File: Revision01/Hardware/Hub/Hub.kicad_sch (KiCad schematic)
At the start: 26 parts, among them J20 Conn_01x04, J3 Conn_01x04, J4 Conn_01x05, J5 Conn_01x05, SW1 ON/OFF_SW_SPST_LED, U1 NUCLEO-L476RG, U2 LMR51603XFDBVR

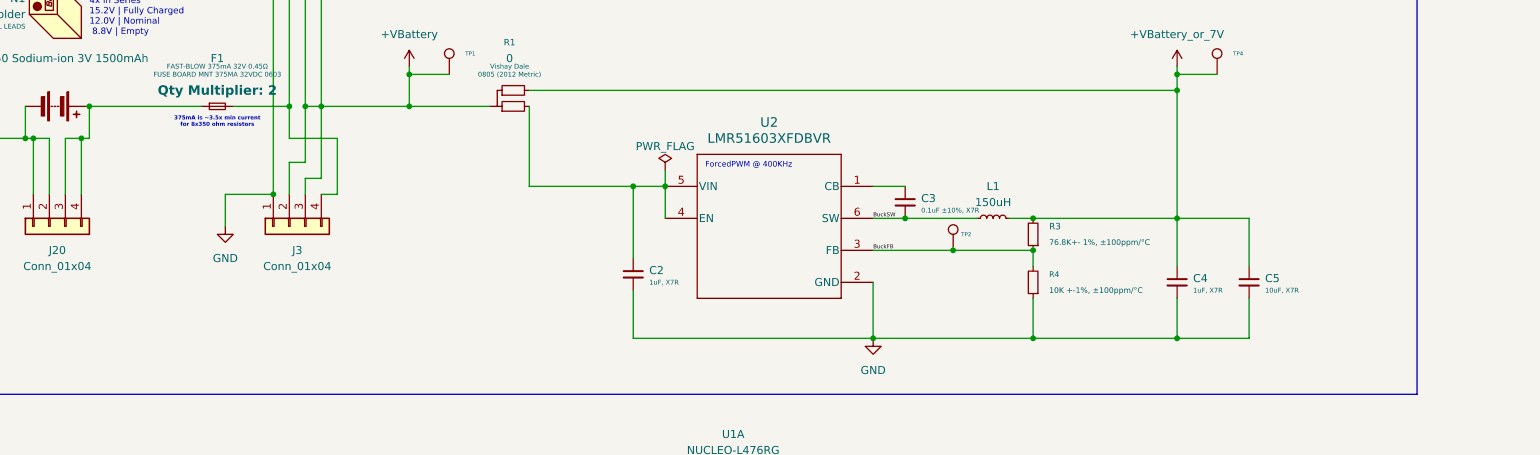
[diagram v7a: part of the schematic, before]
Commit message: . Hub & Amp: Changed wiring standard to GND SIG GND GND PWR GND . Hub: Added GND plane to 3.3V . Hub: Moved 1M pulldown resistor . Hub & Amp: Adjusted thermal relief tolerances . Hub: Changed buck convertor layout so capacitors are inline with feedback pin . Hub: Added stitching vias . Hub & Amp: Changed font sizes, changed silkscreen to be oriented one way
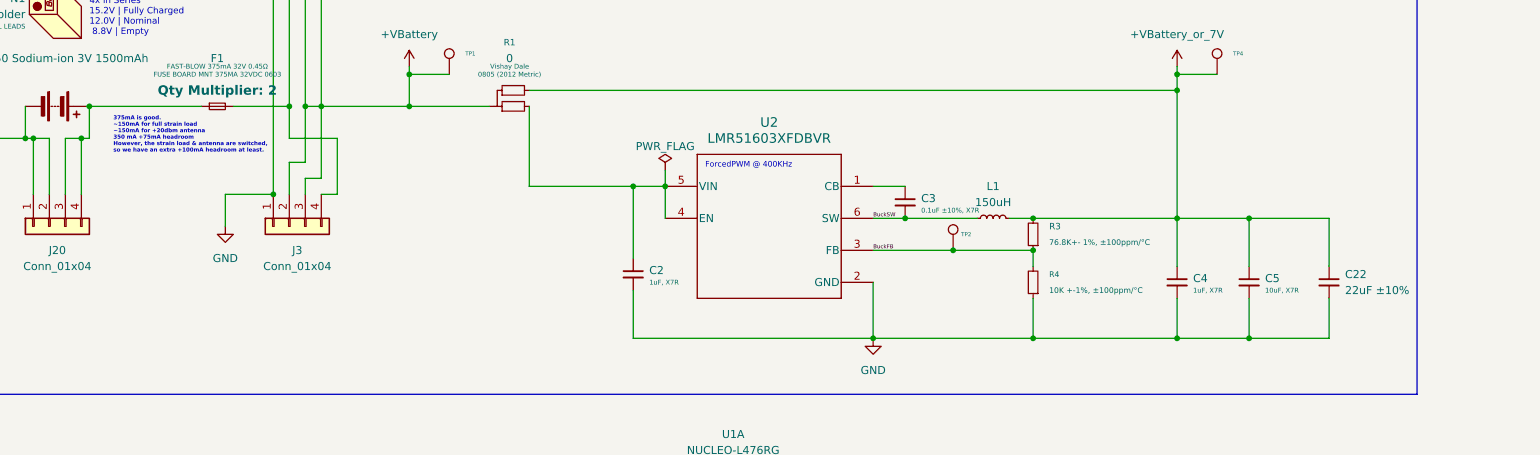
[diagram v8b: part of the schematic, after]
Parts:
- added C22: 22uF ±10%, Capacitor_SMD:C_1206_3216Metric_Pad1.33x1.80mm_HandSolder, symbol Device:C_Small
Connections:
- net +VBattery_or_7V: now also C22.1
- net GND: now also C22.2
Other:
- note added: "375mA is good. ~150mA for full strain load ~150mA for +20dbm antenna 350 mA +75mA headroom However, the strain load & antenna are switched, so we have an extra +100mA headroom at least."
- note removed: "375mA is ~3.5x min current for 8x350 ohm resistors"
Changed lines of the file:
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@@
 		)
 	)
-	(text "375mA is ~3.5x min current\nfor 8x350 ohm resistors"
+	(text "375mA is good.\n~150mA for full strain load \n~150mA for +20dbm antenna\n350 mA +75mA headroom\nHowever, the strain load & antenna are switched,\nso we have an extra +100mA headroom at least."
 		(exclude_from_sim no)
-		(at 71.12 68.58 0)
+		(at 54.61 70.612 0)
 		(effects
 			(font
@@
 				(bold yes)
 			)
+			(justify left)
 		)
 	)
@@
 	)
 	(junction
+		(at 234.95 83.82)
+		(diameter 0)
+		(color 0 0 0 0)
+	)
+	(junction
 		(at 175.26 102.87)
 		(diameter 0)
@@
 	)
 	(junction
+		(at 234.95 102.87)
+		(diameter 0)
+		(color 0 0 0 0)
+	)
+	(junction
 		(at 161.29 264.16)
 		(diameter 0)
@@
 	(wire
 		(pts
+			(xy 247.65 102.87) (xy 247.65 96.52)
+		)
+		(stroke
+			(width 0)
+			(type default)
+		)
+	)
+	(wire
+		(pts
 			(xy 161.29 266.7) (xy 166.37 266.7)
 		)
@@
 	(wire
 		(pts
+			(xy 234.95 102.87) (xy 247.65 102.87)
+		)
+		(stroke
+			(width 0)
+			(type default)
+		)
+	)
+	(wire
+		(pts
 			(xy 307.34 161.29) (xy 311.15 161.29)
 		)
@@
 	(wire
 		(pts
+			(xy 247.65 83.82) (xy 234.95 83.82)
+		)
+		(stroke
+			(width 0)
+			(type default)
+		)
+	)
+	(wire
+		(pts
 			(xy 87.63 80.01) (xy 90.17 80.01)
 		)
@@
 	(wire
 		(pts
+			(xy 247.65 91.44) (xy 247.65 83.82)
+		)
+		(stroke
+			(width 0)
+			(type default)
+		)
+	)
+	(wire
+		(pts
 			(xy 87.63 31.75) (xy 80.01 31.75)
 		)
@@
 					(unit 1)
 				)
+			)
+		)
+	)
+	(symbol
+		(lib_id "Device:C_Small")
+		(at 247.65 93.98 0)
+		(unit 1)
+		(exclude_from_sim no)
+		(in_bom yes)
+		(on_board yes)
+		(dnp no)
+		(fields_autoplaced yes)
+		(property "Reference" "C22"
+			(at 250.19 92.7162 0)
+			(effects
+				(font
+					(size 1.27 1.27)
+				)
+				(justify left)
+			)
+		)
+		(property "Value" "22uF ±10%"
+			(at 250.19 95.2562 0)
+			(effects
+				(font
+					(size 1.27 1.27)
+				)
+				(justify left)
+			)
+		)
+		(property "Footprint" "Capacitor_SMD:C_1206_3216Metric_Pad1.33x1.80mm_HandSolder"
+			(at 247.65 93.98 0)
+			(effects
+				(font
+					(size 1.27 1.27)
+				)
+				(hide yes)
+			)
+		)
+		(property "Datasheet" "https://mm.digikey.com/Volume0/opasdata/d220001/medias/docus/658/CL31A226KAHNNNE_Spec.pdf"
+			(at 247.65 93.98 0)
+			(effects
+				(font
+					(size 1.27 1.27)
+				)
+				(hide yes)
+			)
+		)
+		(property "Description" "CAP CER 22UF 25V X5R 1206"
+			(at 247.65 93.98 0)
+			(effects
+				(font
+					(size 1.27 1.27)
+				)
+				(hide yes)
+			)
+		)
+		(property "Manufacturer Part Number" "CL31A226KAHNNNE"
+			(at 247.65 93.98 0)
+			(effects
+				(font
+					(size 1.27 1.27)
+				)
+				(hide yes)
+			)
+		)
+		(property "Detailed Description" "22 µF ±10% 25V Ceramic Capacitor X5R 1206 (3216 Metric)"
+			(at 247.65 93.98 0)
+			(effects
+				(font
+					(size 1.27 1.27)
+				)
+				(hide yes)
+			)
+		)
+		(property "Manufacturer" "Samsung Electro-Mechanics"
+			(at 247.65 93.98 0)
+			(effects
+				(font
+					(size 1.27 1.27)
+				)
+				(hide yes)
+			)
+		)
+		(property "Qty Multiplier" ""
+			(at 247.65 93.98 0)
+			(effects
+				(font
+					(size 1.27 1.27)
+				)
+			)
+		)
+		(property "Package" "1206 (3216 Metric)"
+			(at 247.65 93.98 0)
+			(effects
+				(font
+					(size 1.27 1.27)
+				)
+				(hide yes)
+			)
+		)
+		(property "DigiKey Link" "https://www.digikey.ca/en/products/detail/samsung-electro-mechanics/CL31A226KAHNNNE/3888705"
+			(at 247.65 93.98 0)
+			(effects
+				(font
+					(size 1.27 1.27)
+				)
+				(hide yes)
+			)
+		)
+		(property "DigiKey Part Number" "1276-3047-1-ND "
+			(at 247.65 93.98 0)
+			(effects
+				(font
+					(size 1.27 1.27)
+				)
+				(hide yes)
+			)
+		)
+		(property "AliExpress Link" ""
+			(at 247.65 93.98 0)
+			(effects
+				(font
+					(size 1.27 1.27)
+				)
+				(hide yes)
+			)
+		)
+		(property "AliExpress Part Number" ""
+			(at 247.65 93.98 0)
+			(effects
+				(font
+					(size 1.27 1.27)
+				)
+				(hide yes)
+			)
+		)
+		(property "Mouser Link" "https://www.mouser.ca/ProductDetail/Samsung-Electro-Mechanics/CL31A226KAHNNNE?qs=X6jEic%2FHinCdwsjGJII51w%3D%3D"
+			(at 247.65 93.98 0)
+			(effects
+				(font
+					(size 1.27 1.27)
+				)
+				(hide yes)
+			)
+		)
+		(property "Mouser Part Number" "187-CL31A226KAHNNNE "
+			(at 247.65 93.98 0)
+			(effects
+				(font
+					(size 1.27 1.27)
+				)
+				(hide yes)
+			)
+		)
+		(pin "2"
+		)
+		(pin "1"
+		)
+		(instances
+			(project "Hub"
+				(path "/955cc99e-a129-42cf-abc7-aa99813fdb5f"
+					(reference "C22")
+					(unit 1)
+				)
